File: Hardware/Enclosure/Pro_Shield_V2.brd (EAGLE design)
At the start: 58.4 x 58.4 mm, 9 parts, among them J1 ARDUINO_R3_SHIELD

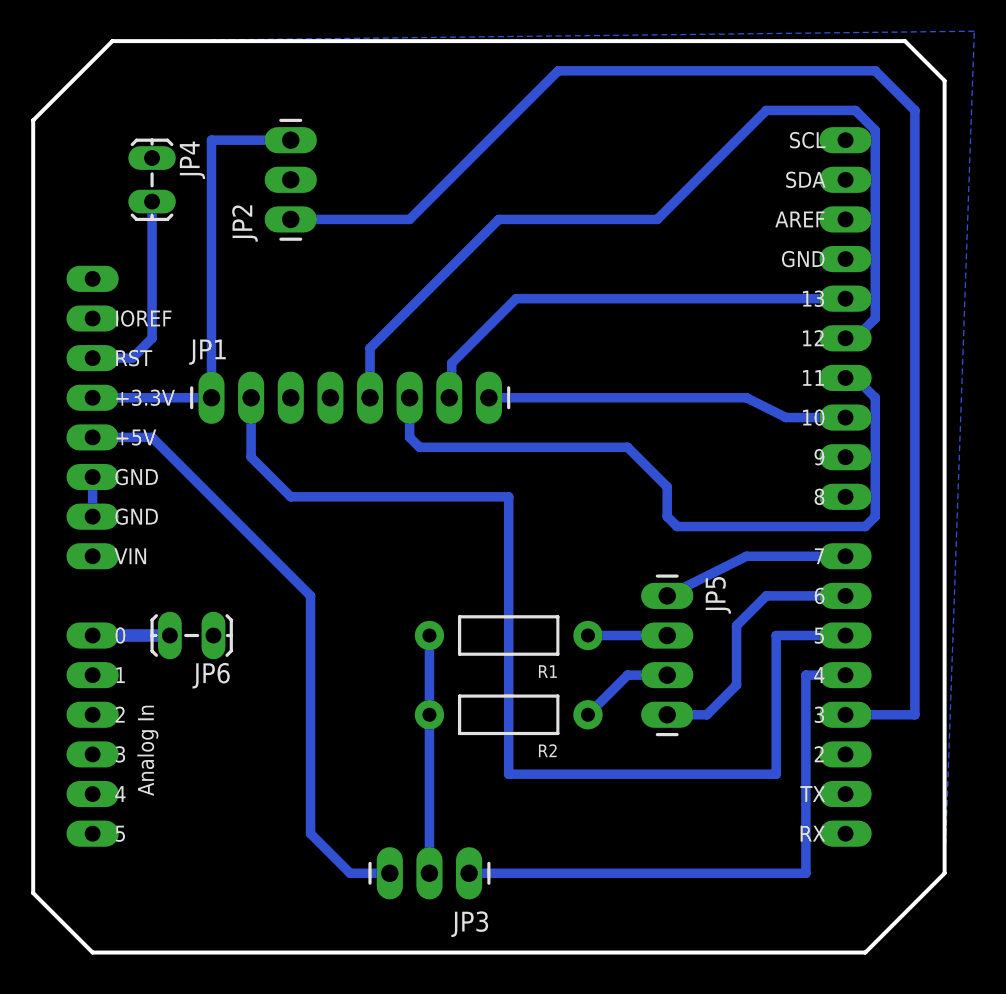
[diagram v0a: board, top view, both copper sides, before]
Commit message: New boards, terminal enclosures, and labview interface
Former-commit-id: 246ca6c8f016e846ca299188d99d46875b994b37
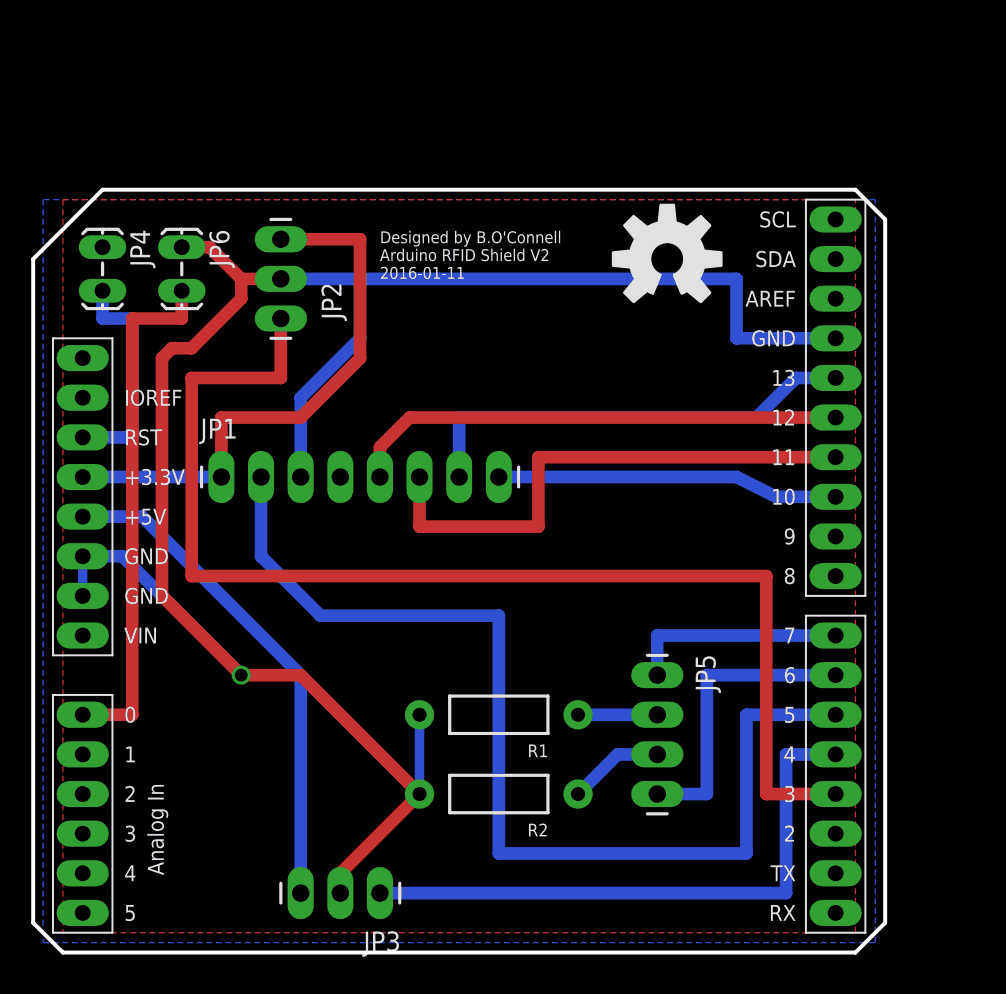
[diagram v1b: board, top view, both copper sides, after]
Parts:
- added U$1: (no value), SparkFun-Aesthetics:OSHW-LOGO-L
- moved JP6 24.8 mm to (9.53, 45.1), turned to 270 degrees
- moved JP4 6.54 mm to (4.45, 45.1)
- moved JP2 6.38 mm to (15.9, 40.6)
- moved JP3 5.85 mm to (22.2, 3.81)
- moved JP1 5.12 mm to (12.1, 30.5)
- moved R1 5.12 mm to (29.8, 15.2)
- moved R2 5.12 mm to (29.8, 10.2)
- moved J1 5.12 mm to (54.0, 57.1)
- moved JP5 5.12 mm to (40.0, 17.8)
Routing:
- net GND: track 17.8 -> 135.2 mm, vias 0 -> 1
- net OVRD: track 5.21 -> 33.5 mm
- net MISO: track 56.9 -> 31.9 mm
- net MOSI: track 46.2 -> 34.3 mm
- net LCD_RX: track 88.2 -> 77.5 mm
- net 5V: track 39.6 -> 32.1 mm
- net 3.3V: track 29.2 -> 35.9 mm
- net DEC: track 16.8 -> 19.1 mm
- net RST: track 70.9 -> 68.9 mm
- net APP: track 12.0 -> 14.0 mm
- net RESET: track 13.1 -> 14.5 mm
- net INTLK: track 36.8 -> 38.1 mm
- net SDA: track 23.2 -> 21.9 mm
- added copper zone on layer 1, net GND
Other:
- board size 58.4 x 58.4 mm -> 54.6 x 48.9 mm
- board text added: "Designed by B.O'Connell Arduino RFID Shield V2 2016-01-11"
